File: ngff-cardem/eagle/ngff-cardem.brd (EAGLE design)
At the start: 90 x 100 mm, 148 parts, among them IC1 FPF2109, IC2 FPF2109, IC201 CB3Q3244PW, IC202 CB3Q3244PW, IC203 IP4234CZ6, IC302 TPS22958-DGN, J301 PJ-002BH-SMT-TR, M2 MENTOR_12701001, M3 MENTOR_12701001, Q201 12MHz, T1 BC847, T101 BC847, U201 IP4234CZ6, U202 AT91SAM3S-AU, U301 MIC5366-1.8YC5, X1 PINHD-2X3-SP, X102 ZX360D-B-10P(30), X201 MINI-USB-SHIELD-UX60-MB-5ST, X202 2.54mm, X3 JACK2.5_SJ-2523, X301 22-23-2041

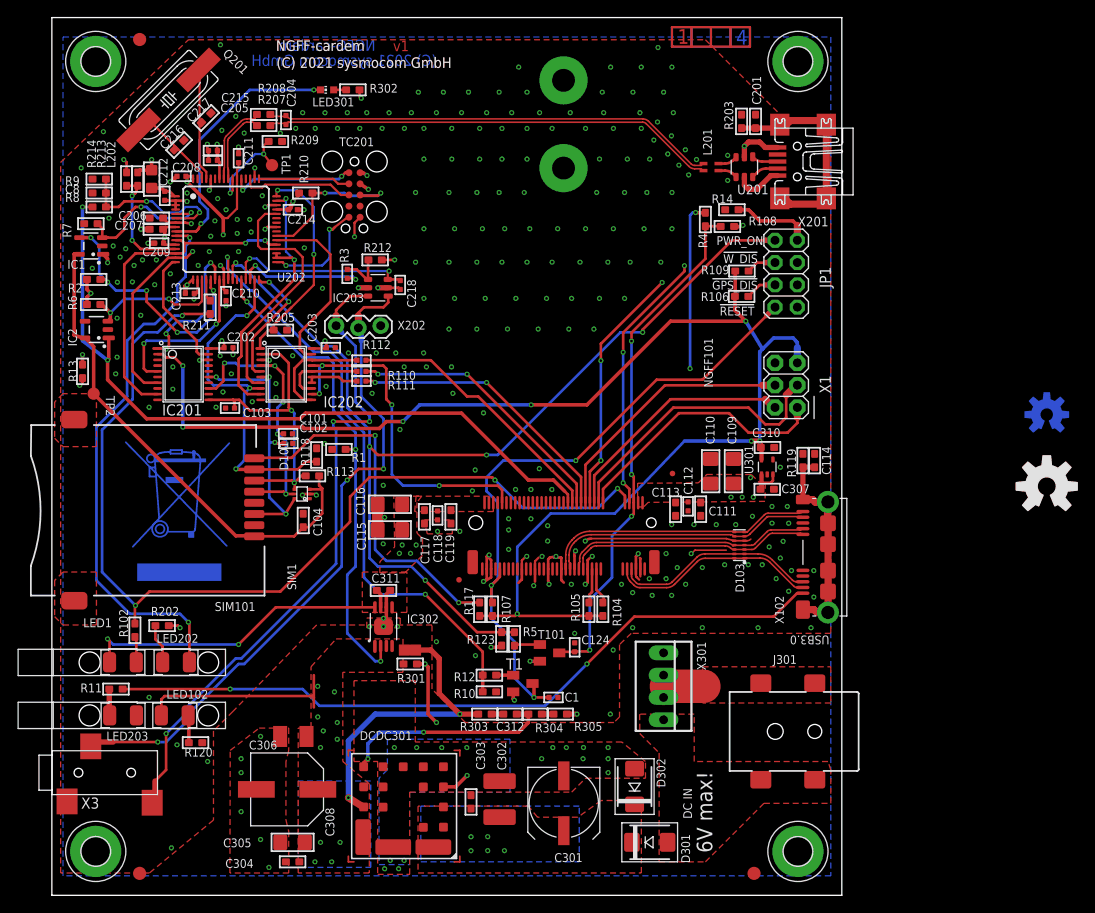
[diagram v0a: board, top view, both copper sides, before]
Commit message: ngff-cardem: length matching for USB3
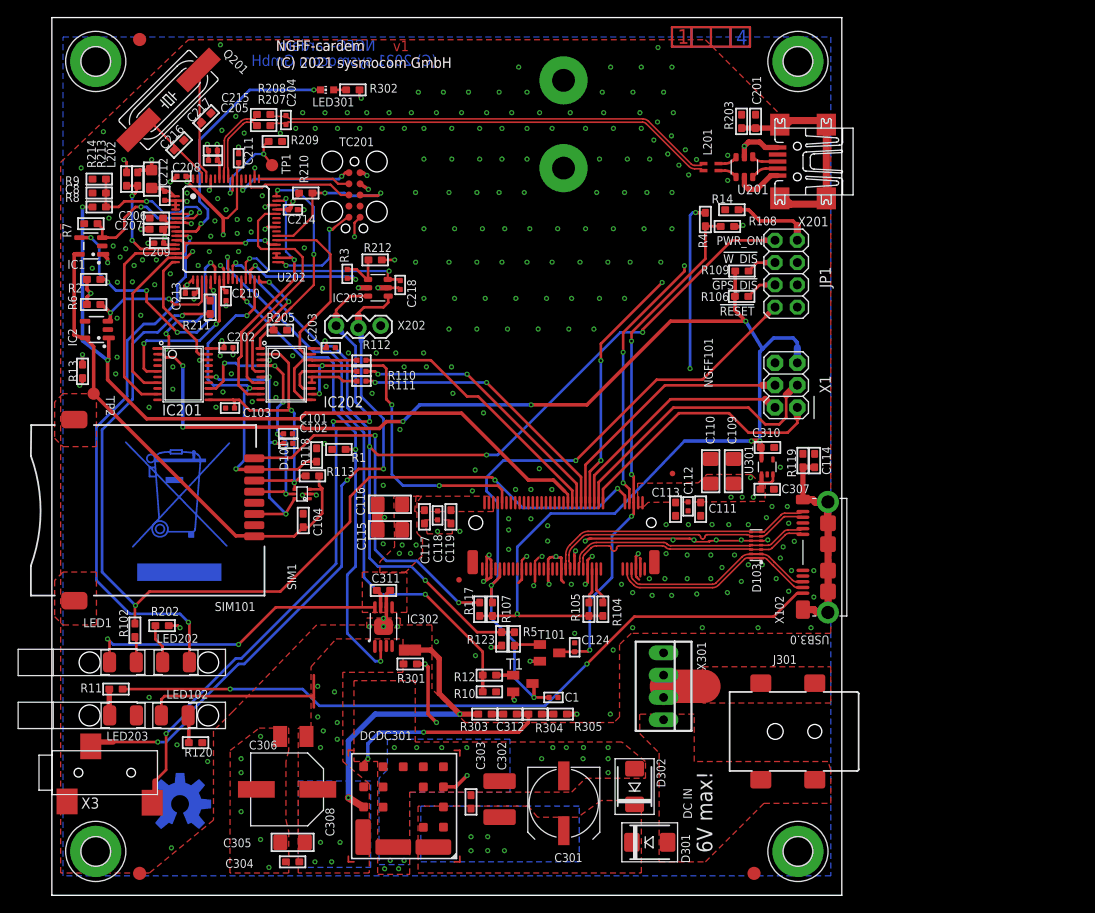
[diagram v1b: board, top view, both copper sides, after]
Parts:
- removed U$3: (no value), SparkFun-Aesthetics:OSHW-LOGO-M_COPPER
- removed U$4: (no value), SparkFun-Aesthetics:OSHW-LOGO-M
- moved LOGO1 105.2 mm to (14.6, 10.4), flipped to the bottom
- moved U$7 105.2 mm to (14.6, 10.4), flipped to the bottom
- moved D103 1.91 mm to (80.2, 39.9)
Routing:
- net _NGFF_USB_D_N: track 23.9 -> 25.4 mm
- net _NGFF_USB_D_P: track 23.2 -> 24.6 mm
- net GND: track 109.0 -> 107.6 mm, vias 292 -> 301
- net USB3.0_TX_N: track 27.7 -> 28.3 mm

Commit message: ngff-cardem: ERC+DRC done
missing is a single ERC issue related to the floppy conn which
has to change its position and to a 90° type.
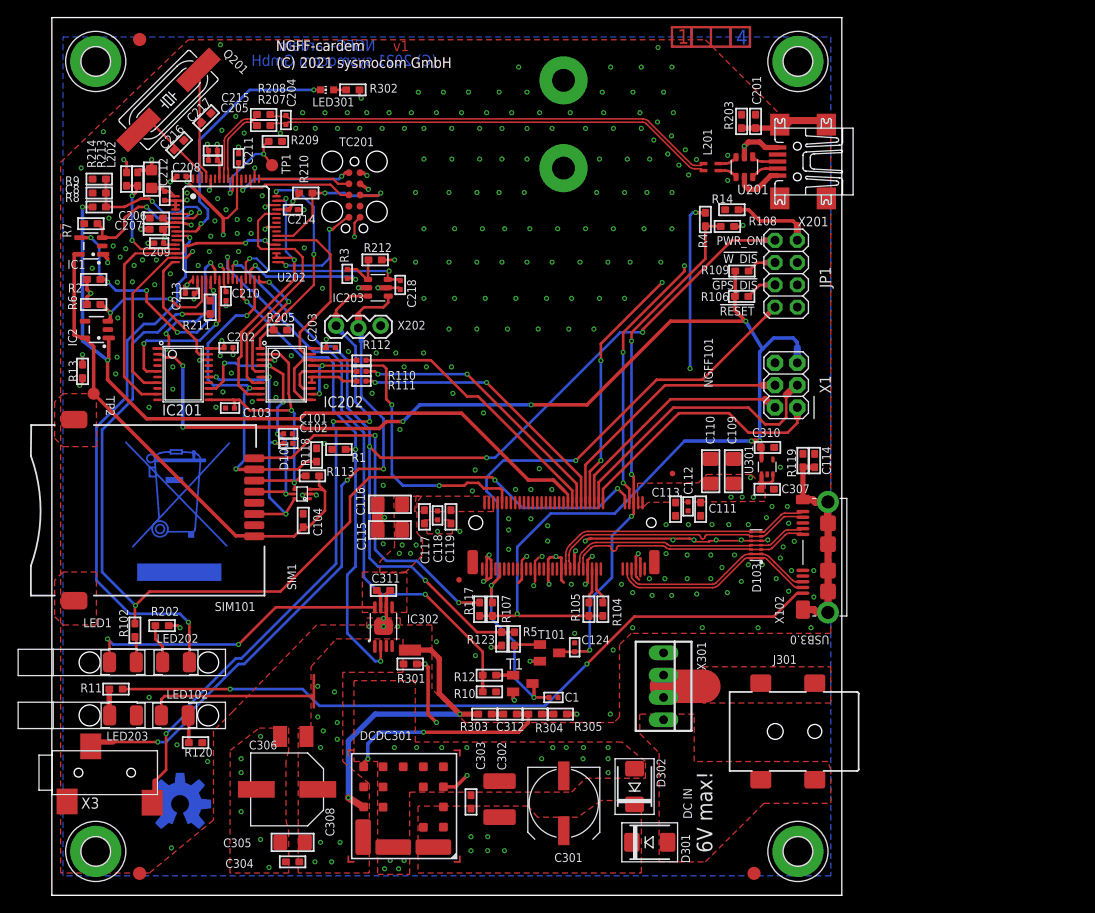
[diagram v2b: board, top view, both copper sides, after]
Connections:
- net N$9: no longer X201.M2, X201.M3
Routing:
- net N$9: track 26.1 -> 12.0 mm
- net N$5: track 10.9 -> 12.5 mm
- net SLOT_CLK: track 32.7 -> 31.9 mm
- net SLOT_VDD: track 57.6 -> 58.2 mm
- removed copper zone on layer 16, net +VIN_PROT
- removed copper zone on layer 16, net VCC_3V3

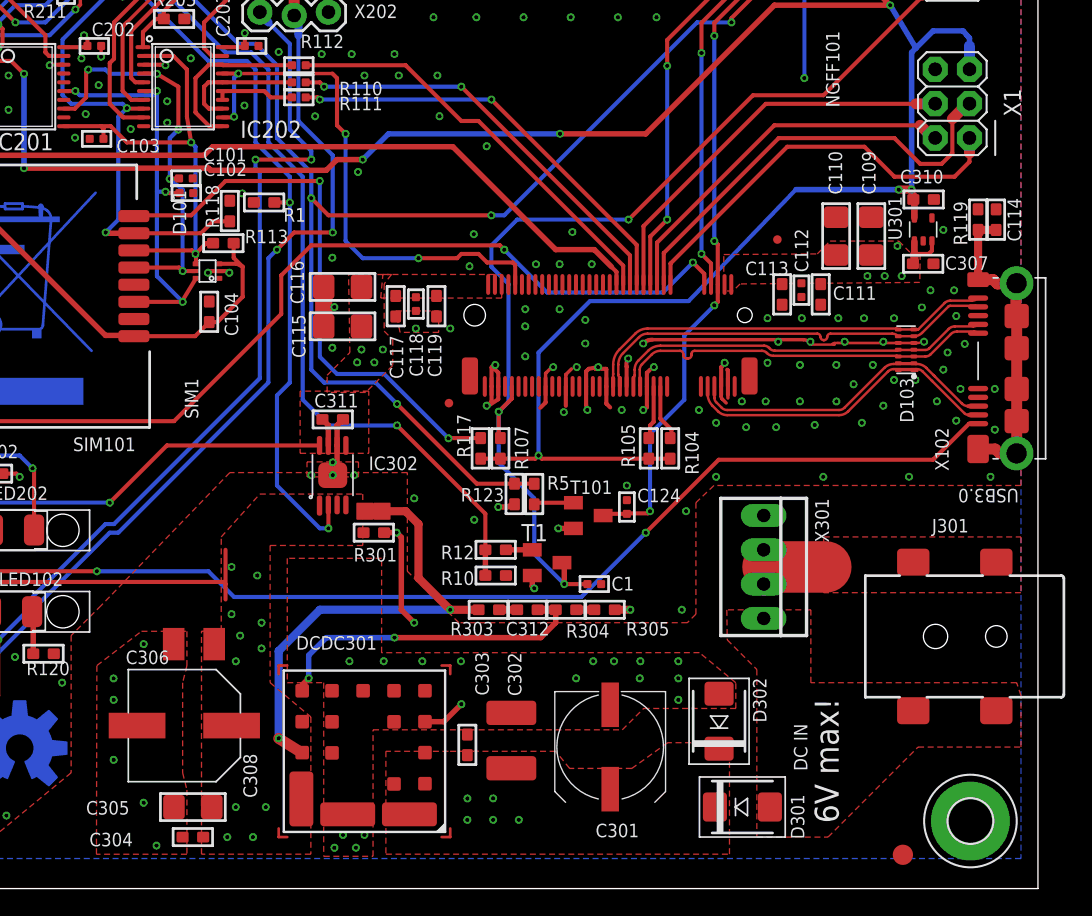
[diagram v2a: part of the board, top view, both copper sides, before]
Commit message: ngff-cardem: prelim floppy power connector
Generic RA 2,5mm 1x4 header w/ similar plastics
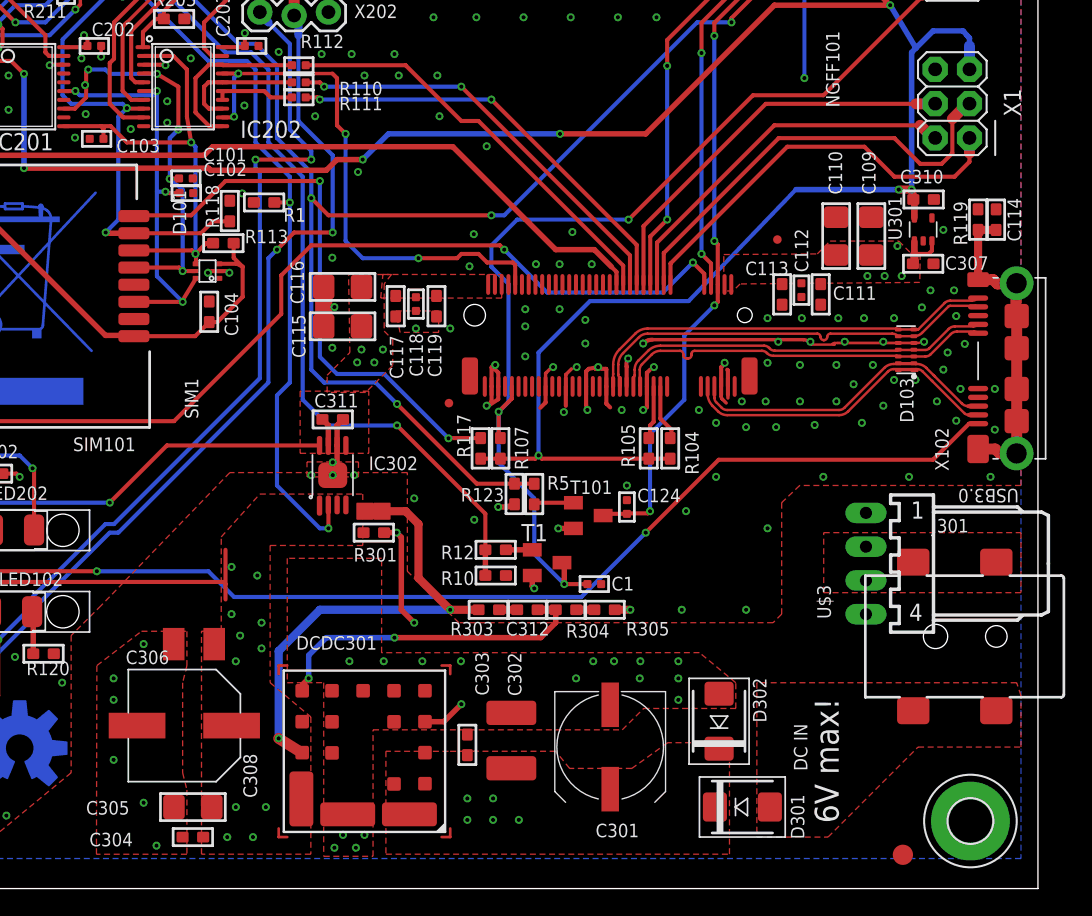
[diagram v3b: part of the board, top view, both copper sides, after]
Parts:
- removed X301: 22-23-2041, con-molex:22-23-2041
- added U$3: 171826-4-RA, 171826-4:171826-4
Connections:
- net +VIN: now also U$3.4; no longer X301.4
- net GND: now also U$3.2, U$3.3; no longer X301.2, X301.3
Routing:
- net GND: track 107.6 -> 98.3 mm, vias 301 -> 303
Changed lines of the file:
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@@
 <grid distance="0.3175" unitdist="mm" unit="mm" style="lines" multiple="1" display="no" altdistance="0.15875" altunitdist="mm" altunit="mm"/>
 <layers>
-<layer number="1" name="Top" color="4" fill="1" visible="yes" active="yes"/>
-<layer number="2" name="Route2" color="3" fill="3" visible="yes" active="yes"/>
+<layer number="1" name="Top" color="4" fill="1" visible="no" active="yes"/>
+<layer number="2" name="Route2" color="3" fill="3" visible="no" active="yes"/>
 <layer number="3" name="Route3" color="4" fill="3" visible="no" active="no"/>
 <layer number="4" name="Route4" color="1" fill="4" visible="no" active="no"/>
@@
 <layer number="13" name="Route13" color="4" fill="5" visible="no" active="no"/>
 <layer number="14" name="Route14" color="1" fill="6" visible="no" active="no"/>
-<layer number="15" name="Route15" color="14" fill="6" visible="yes" active="yes"/>
-<layer number="16" name="Bottom" color="1" fill="1" visible="yes" active="yes"/>
+<layer number="15" name="Route15" color="14" fill="6" visible="no" active="yes"/>
+<layer number="16" name="Bottom" color="1" fill="1" visible="no" active="yes"/>
 <layer number="17" name="Pads" color="2" fill="1" visible="yes" active="yes"/>
-<layer number="18" name="Vias" color="2" fill="1" visible="yes" active="yes"/>
+<layer number="18" name="Vias" color="2" fill="1" visible="no" active="yes"/>
 <layer number="19" name="Unrouted" color="6" fill="1" visible="yes" active="yes"/>
 <layer number="20" name="Dimension" color="15" fill="1" visible="yes" active="yes"/>
-<layer number="21" name="tPlace" color="7" fill="1" visible="no" active="yes"/>
+<layer number="21" name="tPlace" color="7" fill="1" visible="yes" active="yes"/>
 <layer number="22" name="bPlace" color="7" fill="1" visible="no" active="yes"/>
-<layer number="23" name="tOrigins" color="15" fill="1" visible="yes" active="yes"/>
-<layer number="24" name="bOrigins" color="15" fill="1" visible="yes" active="yes"/>
+<layer number="23" name="tOrigins" color="15" fill="1" visible="no" active="yes"/>
+<layer number="24" name="bOrigins" color="15" fill="1" visible="no" active="yes"/>
 <layer number="25" name="tNames" color="7" fill="1" visible="yes" active="yes"/>
-<layer number="26" name="bNames" color="7" fill="1" visible="yes" active="yes"/>
+<layer number="26" name="bNames" color="7" fill="1" visible="no" active="yes"/>
 <layer number="27" name="tValues" color="7" fill="1" visible="no" active="yes"/>
 <layer number="28" name="bValues" color="7" fill="1" visible="no" active="yes"/>
@@
 <layer number="37" name="tTest" color="7" fill="1" visible="no" active="yes"/>
 <layer number="38" name="bTest" color="7" fill="1" visible="no" active="yes"/>
-<layer number="39" name="tKeepout" color="4" fill="11" visible="yes" active="yes"/>
-<layer number="40" name="bKeepout" color="1" fill="11" visible="yes" active="yes"/>
-<layer number="41" name="tRestrict" color="4" fill="10" visible="yes" active="yes"/>
-<layer number="42" name="bRestrict" color="1" fill="10" visible="yes" active="yes"/>
-<layer number="43" name="vRestrict" color="2" fill="10" visible="yes" active="yes"/>
+<layer number="39" name="tKeepout" color="4" fill="11" visible="no" active="yes"/>
+<layer number="40" name="bKeepout" color="1" fill="11" visible="no" active="yes"/>
+<layer number="41" name="tRestrict" color="4" fill="10" visible="no" active="yes"/>
+<layer number="42" name="bRestrict" color="1" fill="10" visible="no" active="yes"/>
+<layer number="43" name="vRestrict" color="2" fill="10" visible="no" active="yes"/>
 <layer number="44" name="Drills" color="7" fill="1" visible="no" active="yes"/>
 <layer number="45" name="Holes" color="7" fill="1" visible="no" active="yes"/>
@@
 <layer number="49" name="Reference" color="7" fill="1" visible="no" active="yes"/>
 <layer number="50" name="dxf" color="7" fill="1" visible="no" active="no"/>
-<layer number="51" name="tDocu" color="7" fill="1" visible="no" active="yes"/>
+<layer number="51" name="tDocu" color="7" fill="1" visible="yes" active="yes"/>
 <layer number="52" name="bDocu" color="7" fill="1" visible="no" active="yes"/>
 <layer number="53" name="tGND_GNDA" color="7" fill="9" visible="no" active="no"/>
@@
 <attribute name="VALUE" x="39.37" y="36.2273" size="0.508" layer="27" font="vector" ratio="10" rot="R180"/>
 </element>
-<element name="X301" library="con-molex" package="22-23-2041" value="22-23-2041" x="69.6925" y="23.8125" rot="R270">
-<attribute name="MF" value="MOLEX" x="69.6925" y="23.8125" size="1.778" layer="27" rot="R270" display="off"/>
-<attribute name="OC_FARNELL" value="1462920" x="69.6925" y="23.8125" size="1.778" layer="27" rot="R270" display="off"/>
-<attribute name="MPN" value="22-23-2041" x="69.6925" y="23.8125" size="1.778" layer="27" rot="R270" display="off"/>
-<attribute name="OC_NEWARK" value="38C0355" x="69.6925" y="23.8125" size="1.778" layer="27" rot="R270" display="off"/>
-<attribute name="DESCRIPTION" value="NO DESCRIPTION" x="69.6925" y="23.8125" size="1.778" layer="27" rot="R270" display="off"/>
-<attribute name="MANUFACTURER" value="UNKNOWN MANUFACTURER" x="69.6925" y="23.8125" size="1.778" layer="27" rot="R270" display="off"/>
-<attribute name="MANUFACTURERPARTNUMBER" value="UNKNOWN MANUFACTURER PART NUMBER" x="69.6925" y="23.8125" size="1.778" layer="27" rot="R270" display="off"/>
-<attribute name="SOURCE" value="UNKNOWN SOURCE" x="69.6925" y="23.8125" size="1.778" layer="27" rot="R270" display="off"/>
-<attribute name="SOURCEPARTNUMBER" value="UNKNOWN SOURCE PART NUMBER" x="69.6925" y="23.8125" size="1.778" layer="27" rot="R270" display="off"/>
-<attribute name="ROHSCERTIFICATE" value="UNKNOWN ROHS CERTIFICATE" x="69.6925" y="23.8125" size="1.778" layer="27" rot="R270" display="off"/>
-<attribute name="POPULATED" value="TRUE" x="69.6925" y="23.8125" size="1.778" layer="27" rot="R270" display="off"/>
-<attribute name="CLASS" value="CONNECTOR" x="69.6925" y="23.8125" size="1.778" layer="27" rot="R270" display="off"/>
-<attribute name="LINK" value="UNKNOWN LINK" x="69.6925" y="23.8125" size="1.778" layer="27" rot="R270" display="off"/>
-</element>
 <element name="C308" library="Wurth_Elektronik_Passive_Capacitors_rev15a" package="4.2X1.9X2.8(BXCXA)" value="330u" x="26.7975" y="12.065" smashed="yes">
 <attribute name="CLASS" value="CAPACITOR" x="26.7975" y="12.065" size="1.778" layer="27" display="off"/>
@@
 </element>
 <element name="U$7" library="SparkFun-Aesthetics" package="OSHW-LOGO-L" value="" x="14.605" y="10.3975" rot="MR0"/>
+<element name="U$3" library="171826-4" package="171826-4" value="171826-4-RA" x="82.265" y="24.065" smashed="yes" rot="R90">
+<attribute name="NAME" x="74.6704" y="19.9674" size="1.016" layer="25" ratio="10" rot="R90"/>
+<attribute name="VALUE" x="79.6249" y="30.0071" size="0.8128" layer="27" ratio="10"/>
+</element>
 </elements>
 <signals>
@@
 <contactref element="J301" pad="2"/>
 <polygon width="0.6096" layer="1">
-<vertex x="74.1375" y="26.035"/>
-<vertex x="88.7425" y="26.035"/>
+<vertex x="74.1375" y="26.3525"/>
+<vertex x="88.7425" y="26.3525"/>
 <vertex x="88.7425" y="21.9075"/>
 <vertex x="74.1375" y="21.9075"/>
@@
 <via x="23.78125" y="18.1025" extent="1-16" drill="0.3"/>
 <via x="21.55875" y="13.975" extent="1-16" drill="0.3"/>
-<contactref element="X301" pad="3"/>
-<contactref element="X301" pad="2"/>
-<wire x1="69.6925" y1="22.5425" x2="69.6925" y2="25.0825" width="1.6764" layer="1"/>
-<wire x1="69.6925" y1="22.5425" x2="69.6925" y2="23.1775" width="1.778" layer="1"/>
-<wire x1="69.6925" y1="23.1775" x2="69.0575" y2="23.8125" width="1.778" layer="1"/>
-<wire x1="69.0575" y1="23.8125" x2="70.01" y2="23.8125" width="1.778" layer="1"/>
 <contactref element="IC201" pad="10"/>
 <contactref element="IC202" pad="10"/>
@@
 <vertex x="88.7425" y="88.5825"/>
 <vertex x="88.7425" y="29.845"/>
-<vertex x="66.01" y="29.845"/>
-<vertex x="64.675" y="28.575"/>
-<vertex x="64.675" y="20.32"/>
-<vertex x="64.04" y="19.685"/>
+<vertex x="72.36" y="29.845"/>
+<vertex x="71.025" y="28.575"/>
+<vertex x="71.025" y="20.32"/>
+<vertex x="70.39" y="19.685"/>
 <vertex x="47.1175" y="19.685"/>
 <vertex x="43.3075" y="23.495"/>
@@
 <vertex x="1.27" y="2.2225"/>
 </polygon>
-<wire x1="74.295" y1="23.8125" x2="70.01" y2="23.8125" width="3.81" layer="1"/>
 <via x="78.89875" y="85.34375" extent="1-16" drill="0.3"/>
 <wire x1="82.6825" y1="85.1975" x2="81.2675" y2="85.1975" width="0.6" layer="1"/>
@@
 <via x="27.27375" y="61.47075" extent="1-16" drill="0.3"/>
 <via x="19.1775" y="61.47075" extent="1-16" drill="0.3"/>
-<via x="20.4475" y="59.49075" extent="1-16" drill="0.3"/>
+<via x="19.4475" y="59.49075" extent="1-16" drill="0.3"/>
 <via x="13.78" y="60.20075" extent="1-16" drill="0.3"/>
 <via x="13.78" y="57.66075" extent="1-16" drill="0.3"/>
@@
 <wire x1="73.226225" y1="40.276153125" x2="74.93395625" y2="40.276153125" width="0.185" layer="1"/>
 <wire x1="74.93395625" y1="40.276153125" x2="74.93" y2="40.3225" width="0.185" layer="1" curve="-45"/>
+<contactref element="U$3" pad="3"/>
+<contactref element="U$3" pad="2"/>
+<via x="68.39" y="20.6425" extent="1-16" drill="0.3"/>
+<via x="69.9775" y="26.675" extent="1-16" drill="0.3"/>
+<wire x1="80.7675" y1="24.1675" x2="77.265" y2="25.315" width="0" layer="19" extent="1-1"/>
 </signal>
 <signal name="MDM_UIM_CLK">
@@
 <contactref element="J301" pad="1-1"/>
 <polygon width="0.6096" layer="1">
-<vertex x="66.9625" y="20.6375"/>
-<vertex x="66.9925" y="18.415"/>
-<vertex x="69.185" y="16.2225"/>
+<vertex x="69.185" y="15.24"/>
 <vertex x="69.185" y="3.81"/>
 <vertex x="74.455" y="3.81"/>
@@
 <vertex x="88.7425" y="14.2875"/>
 <vertex x="88.425" y="15.24"/>
-<vertex x="73.185" y="15.24"/>
-<vertex x="73.185" y="20.6375"/>
 </polygon>
-<contactref element="X301" pad="4"/>
+<contactref element="U$3" pad="4"/>
+<wire x1="80.7675" y1="13.1675" x2="77.265" y2="20.315" width="0" layer="19" extent="1-1"/>
 </signal>
 <signal name="PSE_OUT1">
